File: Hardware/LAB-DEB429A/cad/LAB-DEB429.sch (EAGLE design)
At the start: 102 parts, among them J1 TSW-132-02-S-D, J2 TSW-132-02-S-D, U1 LAB-ADSM300F, U10 SF-MICROSD, U11 25MPX, U12 LAB-PPS330D, U13 LAB-PPS330D, U14 LAB-PPS330D, U15 SI1143, U16 LAB-PPS330D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

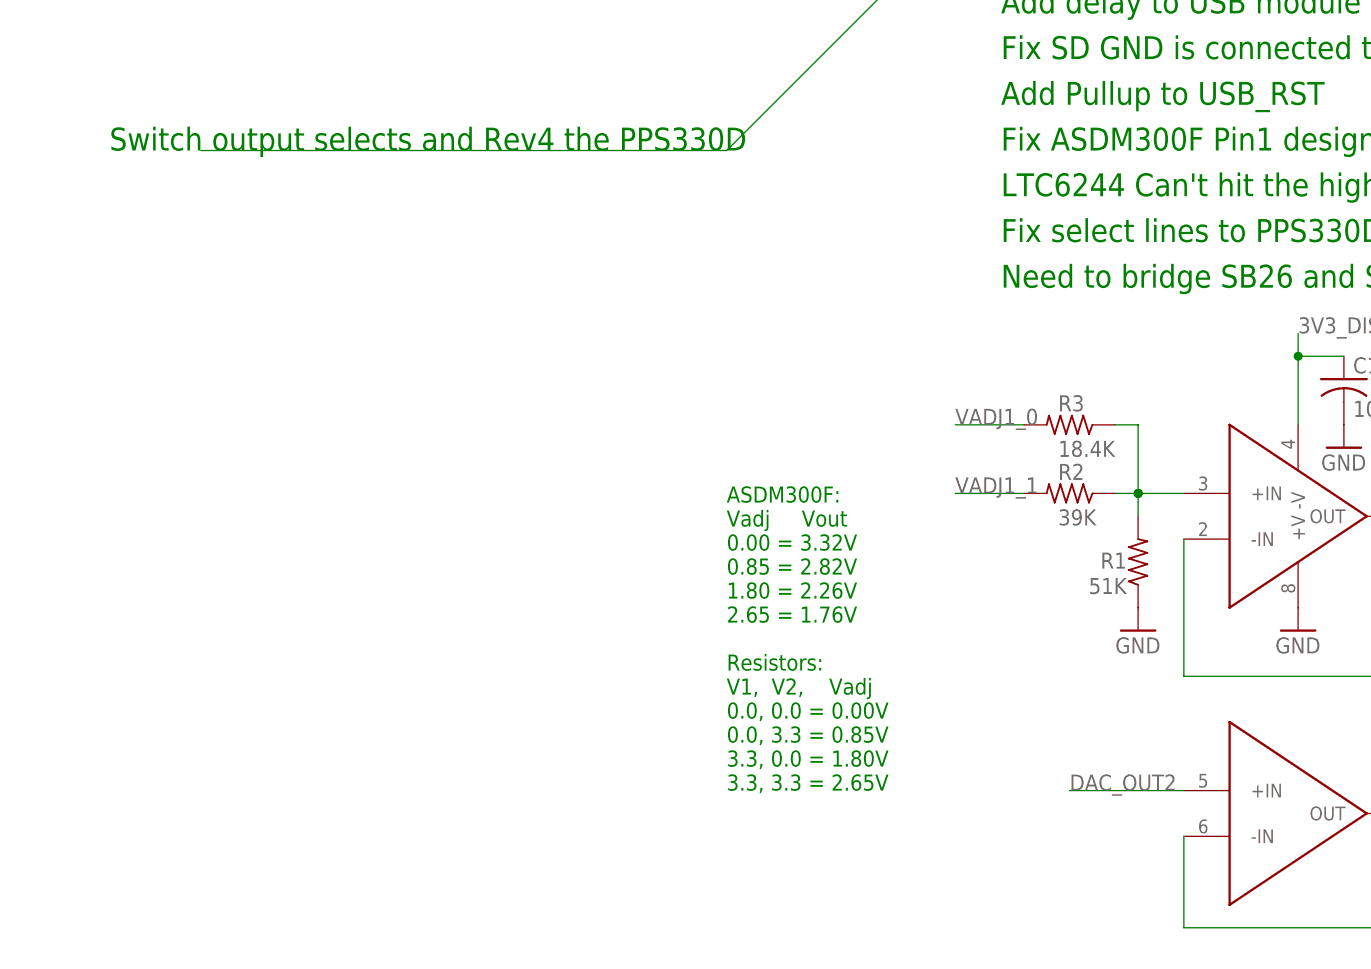
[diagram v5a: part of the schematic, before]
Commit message: 1) Adding some notes to the schematic and bringing out some datasheets.
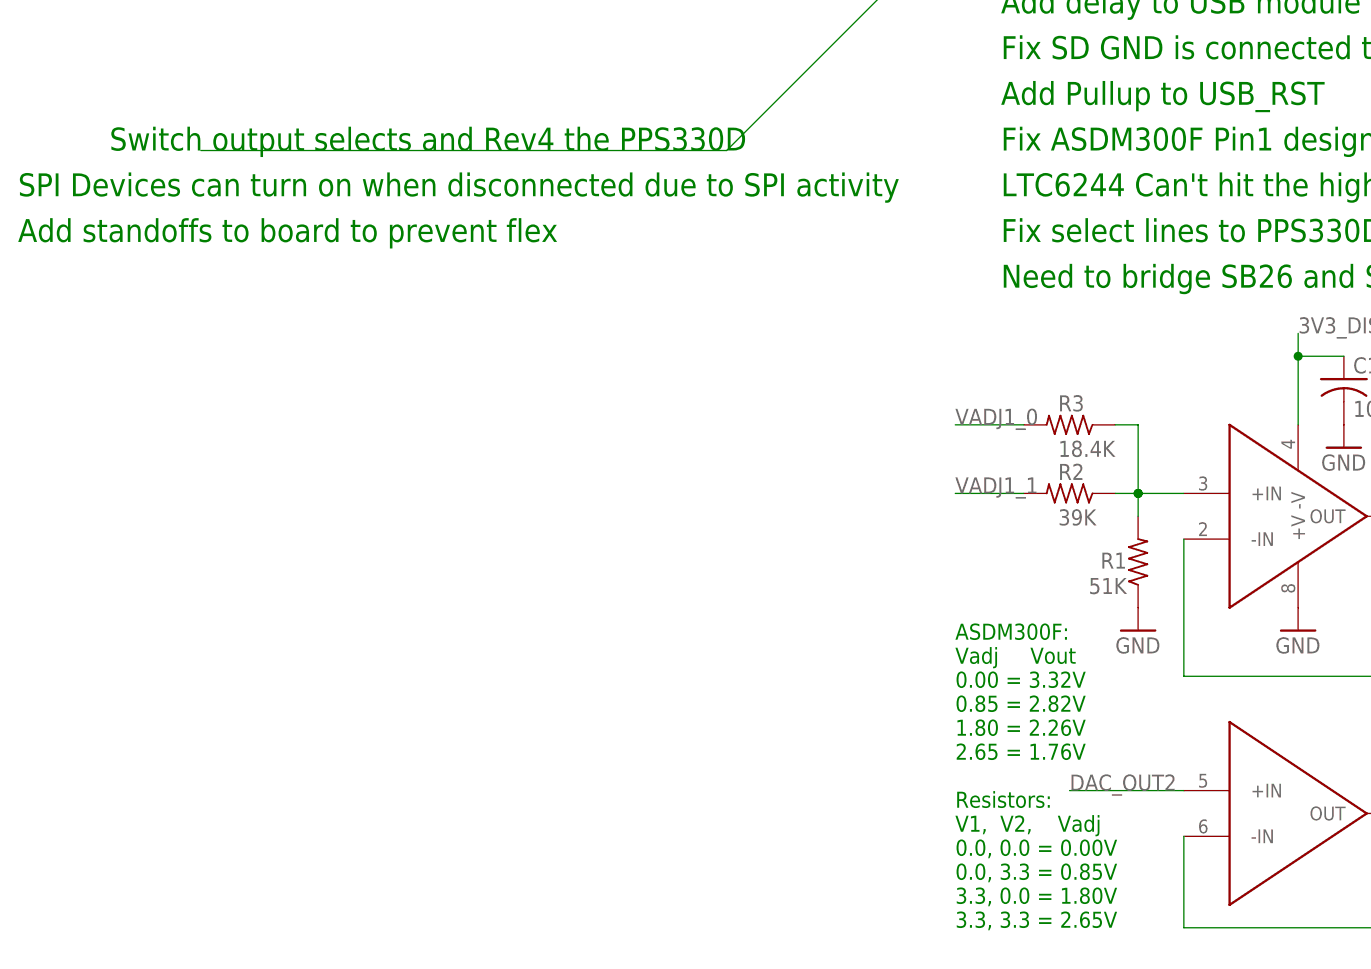
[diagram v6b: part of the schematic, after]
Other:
- note added: "Add standoffs to board to prevent flex"
- note added: "SPI Devices can turn on when disconnected due to SPI activity"
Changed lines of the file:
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@@
 <text x="10.16" y="172.72" size="2.54" layer="91">Can't use LTDC and NAND/NOR flash at the same time.</text>
 <text x="10.16" y="167.64" size="2.54" layer="91">Remove R69 and R72 from DISCO board to remove USB_OTG host circuitry</text>
-<text x="-20.32" y="20.32" size="1.778" layer="91">ASDM300F:
+<text x="5.08" y="5.08" size="1.778" layer="91">ASDM300F:
 Vadj     Vout
 0.00 = 3.32V
@@
 <text x="10.16" y="132.08" size="2.54" layer="91">Need to open collector the SPI chip selects -- use 74HC259</text>
 <text x="10.16" y="182.88" size="2.54" layer="91">May be able to power the MCU off of Vdd pin using a PPS330D</text>
+<text x="-99.06" y="86.36" size="2.54" layer="91">SPI Devices can turn on when disconnected due to SPI activity</text>
+<text x="-99.06" y="81.28" size="2.54" layer="91">Add standoffs to board to prevent flex</text>
 </plain>
 <instances>

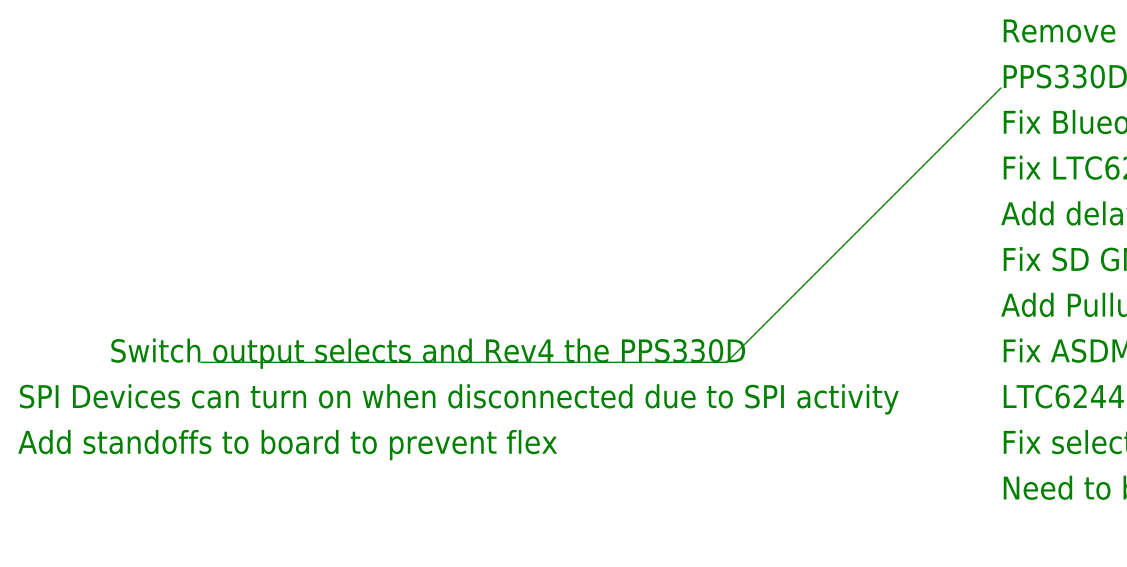
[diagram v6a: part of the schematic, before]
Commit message: 1) Adding a few more findings to the DEB429A schematic.
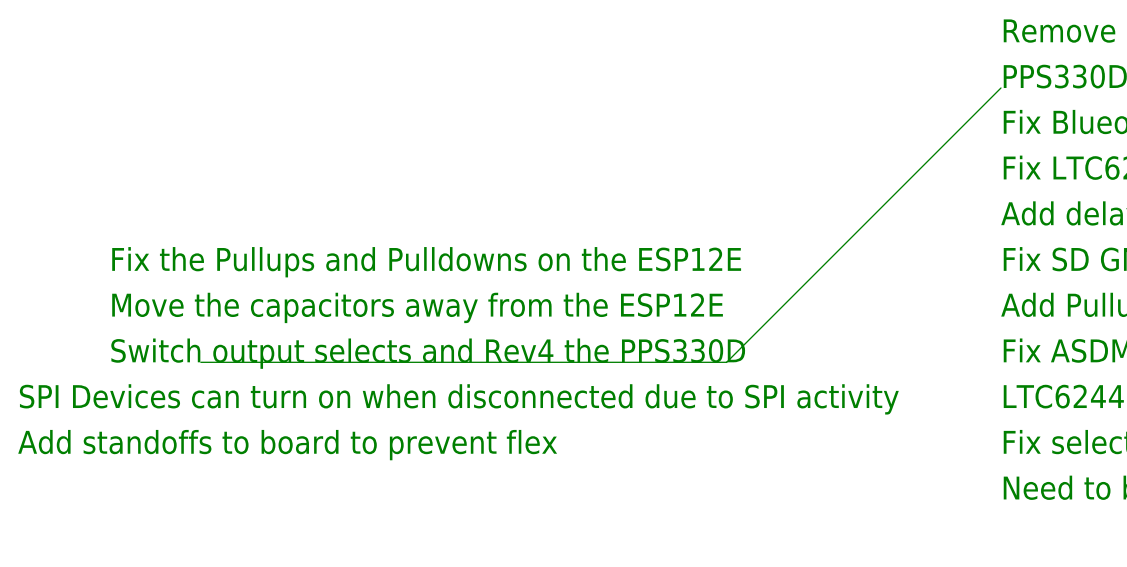
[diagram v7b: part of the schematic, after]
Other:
- note added: "Fix the Pullups and Pulldowns on the ESP12E"
- note added: "Move the capacitors away from the ESP12E"
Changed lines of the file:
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@@
 <text x="-99.06" y="86.36" size="2.54" layer="91">SPI Devices can turn on when disconnected due to SPI activity</text>
 <text x="-99.06" y="81.28" size="2.54" layer="91">Add standoffs to board to prevent flex</text>
+<text x="-88.9" y="96.52" size="2.54" layer="91">Move the capacitors away from the ESP12E</text>
+<text x="-88.9" y="101.6" size="2.54" layer="91">Fix the Pullups and Pulldowns on the ESP12E</text>
 </plain>
 <instances>

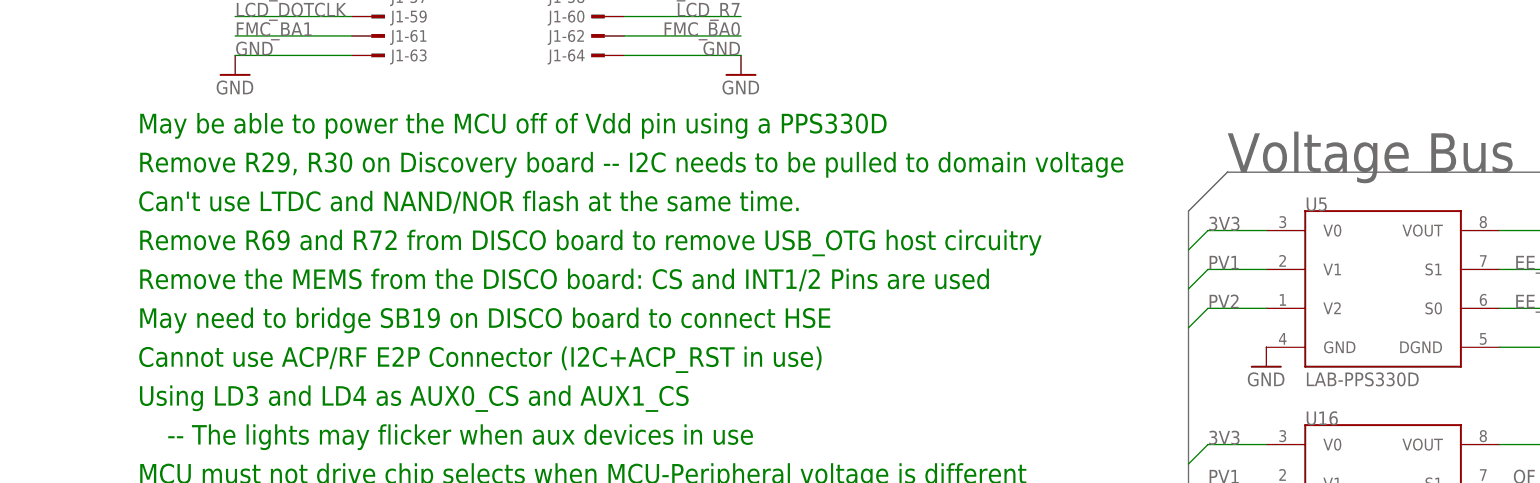
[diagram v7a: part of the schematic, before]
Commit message: 1) Adding C57 to the list of components to remove from the DISCO board (inhibits proper CS of PLR5010D0)
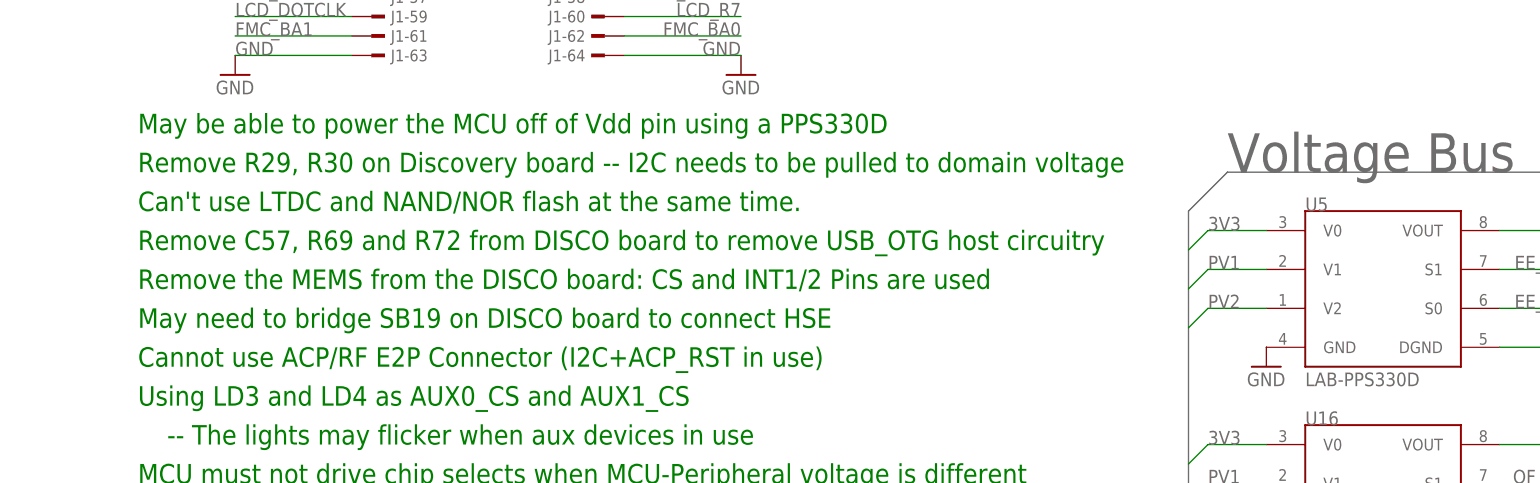
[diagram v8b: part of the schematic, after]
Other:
- note added: "Remove C57, R69 and R72 from DISCO board to remove USB_OTG host circuitry"
- note removed: "Remove R69 and R72 from DISCO board to remove USB_OTG host circuitry"
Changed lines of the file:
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@@
 <text x="10.16" y="177.8" size="2.54" layer="91">Remove R29, R30 on Discovery board -- I2C needs to be pulled to domain voltage</text>
 <text x="10.16" y="172.72" size="2.54" layer="91">Can't use LTDC and NAND/NOR flash at the same time.</text>
-<text x="10.16" y="167.64" size="2.54" layer="91">Remove R69 and R72 from DISCO board to remove USB_OTG host circuitry</text>
+<text x="10.16" y="167.64" size="2.54" layer="91">Remove C57, R69 and R72 from DISCO board to remove USB_OTG host circuitry</text>
 <text x="5.08" y="5.08" size="1.778" layer="91">ASDM300F:
 Vadj     Vout
